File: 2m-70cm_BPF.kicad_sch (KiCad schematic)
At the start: 17 parts, among them J1 Conn_Coaxial, J2 Conn_Coaxial

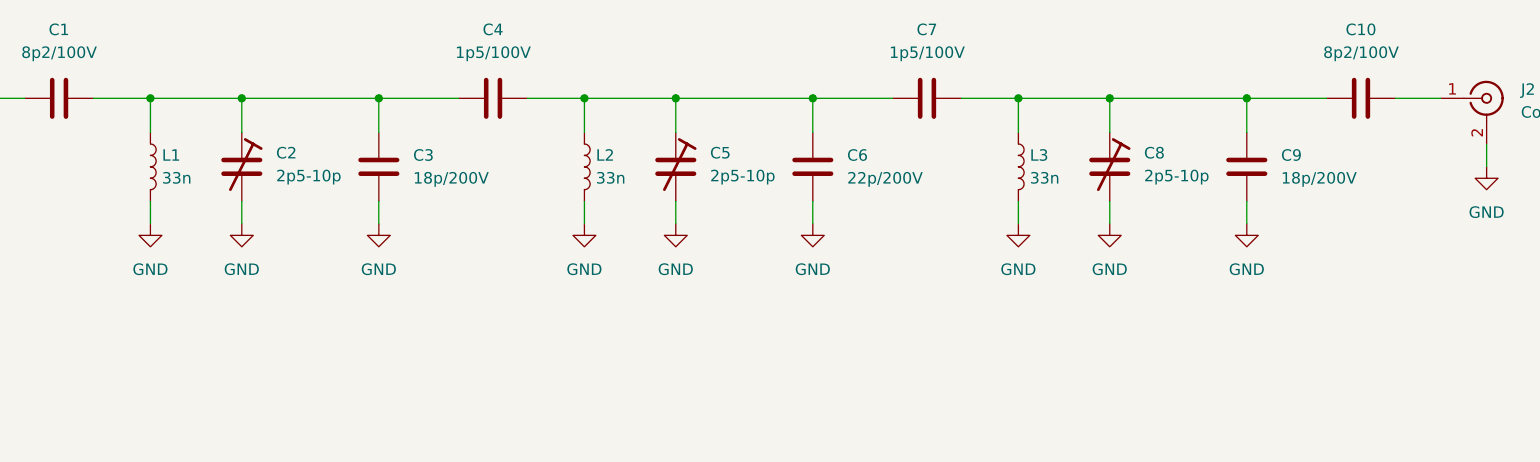
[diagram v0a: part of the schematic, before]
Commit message: Inductors changes to 35n5. Better Q, 2m-137MHz combo.
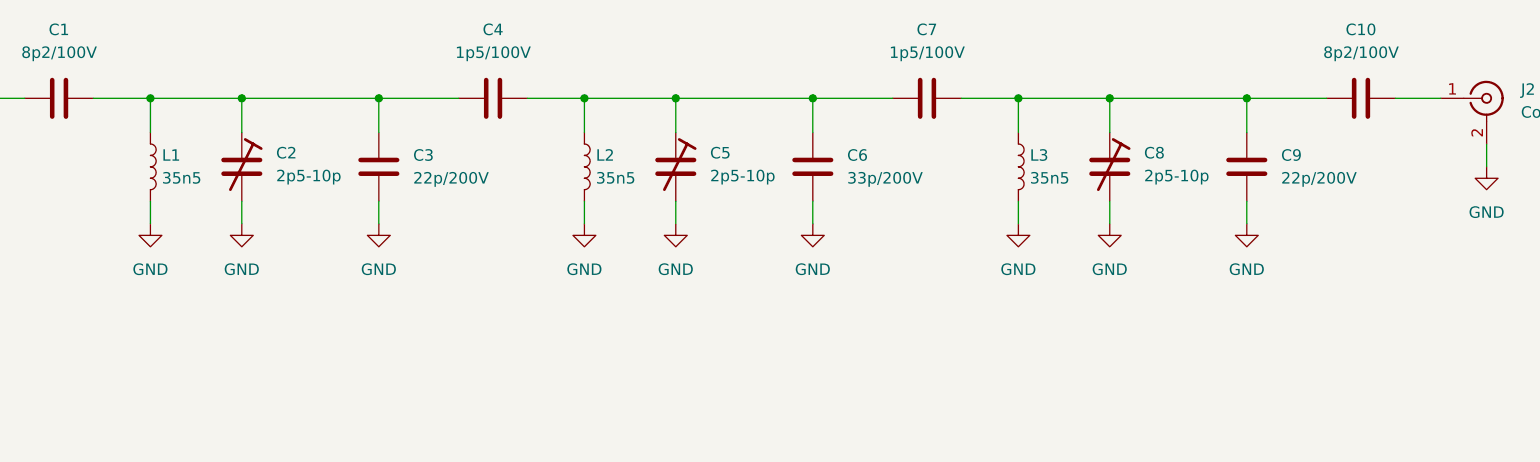
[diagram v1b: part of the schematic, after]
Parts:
- C3, C9: value 18p/200V -> 22p/200V; PN KGQ21HCG2D180FT -> KGQ21HCG2D220FT
- C6: value 22p/200V -> 33p/200V; PN KGQ21HCG2D220FT -> KGQ21HCG2D330FT
- L1, L2, L3: value 33n -> 35n5; footprint riske:L_Wurth_WE-CAIR-4248 -> riske:L_Wurth_WE-CAIR-3168
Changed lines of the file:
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@@
 				)
 			)
-			(table_cell "18p"
+			(table_cell "22p"
 				(exclude_from_sim no)
 				(at 199.39 104.14 0)
@@
 				)
 			)
-			(table_cell "22p"
+			(table_cell "33p"
 				(exclude_from_sim no)
 				(at 199.39 106.68 0)
@@
 				)
 			)
-			(table_cell "33n WE-CAIR 744912133G"
+			(table_cell "35n5 WE-CAIR 744914135G"
 				(exclude_from_sim no)
 				(at 180.34 114.3 0)
@@
 				)
 			)
-			(table_cell "33n WE-CAIR 744912133G"
+			(table_cell "35n5 WE-CAIR 744914135G"
 				(exclude_from_sim no)
 				(at 199.39 114.3 0)
@@
 				)
 			)
-			(table_cell "8n2 WE-CAIR 744911088"
+			(table_cell "8n WE-CAIR 744913080G"
 				(exclude_from_sim no)
 				(at 218.44 114.3 0)
@@
 			)
 		)
-		(property "Value" "33n"
+		(property "Value" "35n5"
 			(at 118.11 77.4699 0)
 			(effects
@@
 			)
 		)
-		(property "Footprint" "riske:L_Wurth_WE-CAIR-4248"
+		(property "Footprint" "riske:L_Wurth_WE-CAIR-3168"
 			(at 116.84 76.2 0)
 			(effects
@@
 			)
 		)
-		(property "Value" "18p/200V"
+		(property "Value" "22p/200V"
 			(at 97.79 77.4699 0)
 			(effects
@@
 			)
 		)
-		(property "PN" "KGQ21HCG2D180FT"
+		(property "PN" "KGQ21HCG2D220FT"
 			(at 93.98 76.2 0)
 			(effects
@@
 			)
 		)
-		(property "Value" "18p/200V"
+		(property "Value" "22p/200V"
 			(at 194.31 77.4699 0)
 			(effects
@@
 			)
 		)
-		(property "PN" "KGQ21HCG2D180FT"
+		(property "PN" "KGQ21HCG2D220FT"
 			(at 190.5 76.2 0)
 			(effects
@@
 			)
 		)
-		(property "Value" "22p/200V"
+		(property "Value" "33p/200V"
 			(at 146.05 77.4699 0)
 			(effects
@@
 			)
 		)
-		(property "PN" "KGQ21HCG2D220FT"
+		(property "PN" "KGQ21HCG2D330FT"
 			(at 142.24 76.2 0)
 			(effects
@@
 			)
 		)
-		(property "Value" "33n"
+		(property "Value" "35n5"
 			(at 166.37 77.4699 0)
 			(effects
@@
 			)
 		)
-		(property "Footprint" "riske:L_Wurth_WE-CAIR-4248"
+		(property "Footprint" "riske:L_Wurth_WE-CAIR-3168"
 			(at 165.1 76.2 0)
 			(effects
@@
 			)
 		)
-		(property "Value" "33n"
+		(property "Value" "35n5"
 			(at 69.85 77.4699 0)
 			(effects
@@
 			)
 		)
-		(property "Footprint" "riske:L_Wurth_WE-CAIR-4248"
+		(property "Footprint" "riske:L_Wurth_WE-CAIR-3168"
 			(at 68.58 76.2 0)
 			(effects
